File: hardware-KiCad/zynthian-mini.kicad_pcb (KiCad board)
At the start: 2 copper layers, 165 x 115 mm, 75 parts, among them SW1 SW_Push, SW10 SW_Push, SW11 SW_Push, SW12 SW_Push, SW13 SW_Push, SW14 SW_Push, SW15 SW_Push, SW16 SW_Push, SW17 SW_Push, SW18 SW_Push, SW19 SW_Push, SW2 SW_Push, SW20 SW_Push, SW3 SW_Push, SW4 SW_Push, SW5 SW_Push, SW6 SW_Push, SW7 SW_Push, SW8 SW_Push, SW9 SW_Push, U1 74HCT14, U2 H11L1M

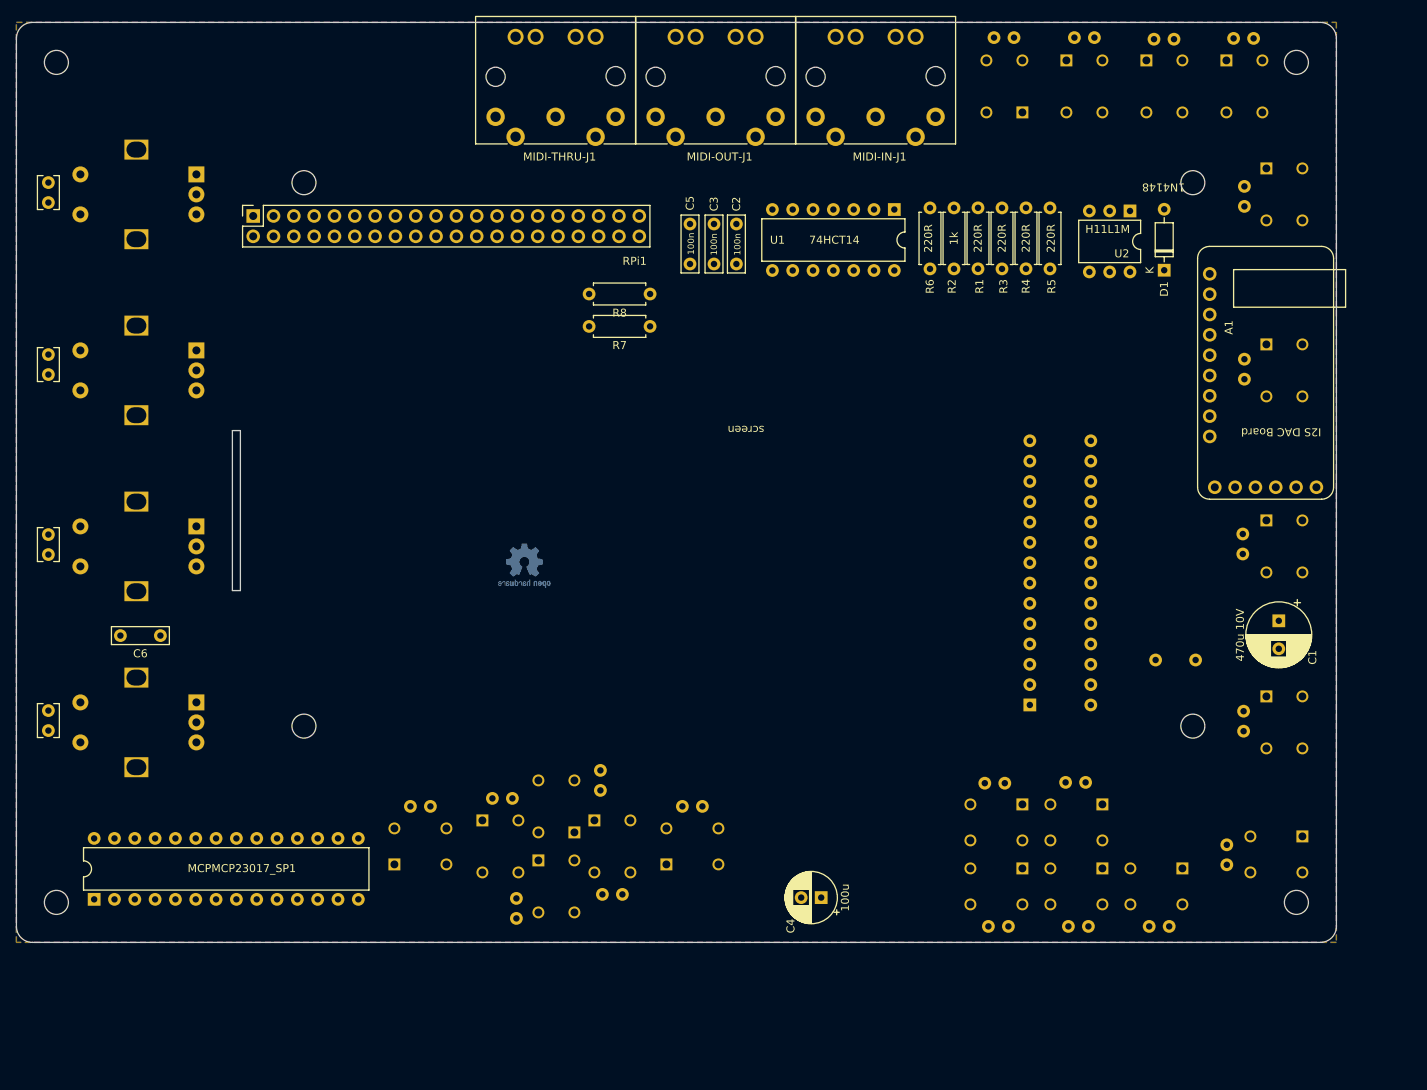
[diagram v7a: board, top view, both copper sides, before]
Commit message: first workable solution for v2 20 pins
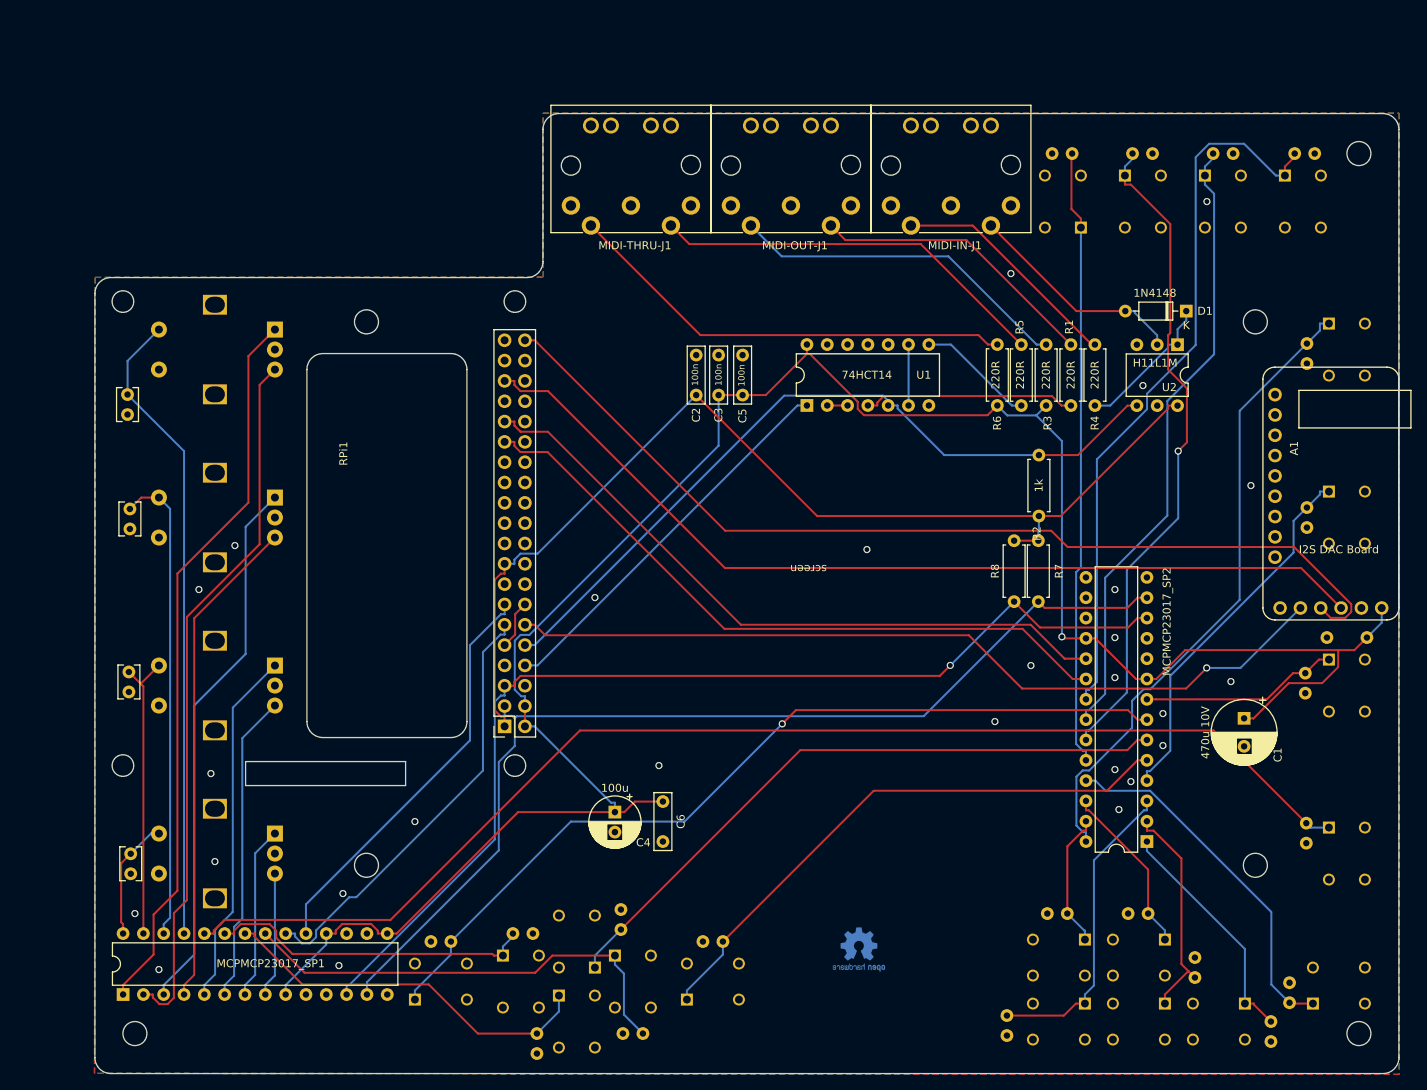
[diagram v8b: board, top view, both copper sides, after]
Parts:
- added G***: MINI v2, project-footprints:Zynthian Logo Mask, B.Cu at (131.4, 148.9)
- Enc1, Enc2, Enc3, Enc4: footprint project-footprints:RotaryEncoder_Alps_EC12E-Switch_Vertical_H20mm -> Rotary_Encoder:RotaryEncoder_Alps_EC12E-Switch_Vertical_H20mm
- MCPMCP23017_SP2: moved to F.Cu
- RPi1: footprint Connector_PinSocket_2.54mm:PinSocket_2x20_P2.54mm_Vertical -> project-footprints:raspberry pi 4 HAT
- moved C6 66.2 mm to (104.4, 121.4), turned to -90 degrees
- moved REF** 63.7 mm to (128.9, 139.9)
- moved R8 59.6 mm to (148.3, 96.4), turned to 90 degrees
- moved R7 59.5 mm to (151.3, 96.4), turned to 90 degrees
- moved R2 32.7 mm to (151.4, 85.7)
- moved RPi1 30.8 mm to (61.4, 77.9)
- moved C13 28.3 mm to (37.5, 70.5)
- moved C4 27.9 mm to (98.4, 122.7), turned to -90 degrees
- moved U1 26.8 mm to (122.4, 71.9), turned to 90 degrees
- moved C7 26.6 mm to (192.4, 100.9), turned to 180 degrees
- moved Enc1 24.2 mm to (55.9, 62.4)
- moved Enc2 23.5 mm to (55.9, 83.4)
- moved Enc3 22.8 mm to (55.9, 104.4)
- moved MCPMCP23017_SP2 22.5 mm to (164.9, 126.4), turned to 180 degrees
- moved Enc4 22.2 mm to (55.9, 125.4)
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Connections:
- D1 pad 1: (no net) -> Net-(D1-K)
- D1 pad 2: (no net) -> Net-(D1-A)
- MCPMCP23017_SP1 pad 11: (no net) -> unconnected-(MCPMCP23017_SP1-NC-Pad11)
- MCPMCP23017_SP1 pad 14: (no net) -> unconnected-(MCPMCP23017_SP1-NC-Pad14)
- MCPMCP23017_SP1 pad 19: (no net) -> INT4
- MCPMCP23017_SP1 pad 20: (no net) -> INT3
- RPi1 pad 15: (no net) -> unconnected-(RPi1-Pin_15-Pad15)
- RPi1 pad 16: (no net) -> unconnected-(RPi1-Pin_16-Pad16)
- RPi1 pad 18: (no net) -> unconnected-(RPi1-Pin_18-Pad18)
- RPi1 pad 19: (no net) -> unconnected-(RPi1-Pin_19-Pad19)
- RPi1 pad 21: (no net) -> unconnected-(RPi1-Pin_21-Pad21)
- RPi1 pad 22: (no net) -> unconnected-(RPi1-Pin_22-Pad22)
- RPi1 pad 23: (no net) -> unconnected-(RPi1-Pin_23-Pad23)
- RPi1 pad 24: (no net) -> unconnected-(RPi1-Pin_24-Pad24)
- RPi1 pad 26: (no net) -> unconnected-(RPi1-Pin_26-Pad26)
- RPi1 pad 27: (no net) -> unconnected-(RPi1-Pin_27-Pad27)
- RPi1 pad 28: (no net) -> unconnected-(RPi1-Pin_28-Pad28)
- RPi1 pad 32: (no net) -> unconnected-(RPi1-Pin_32-Pad32)
- RPi1 pad 33: (no net) -> unconnected-(RPi1-Pin_33-Pad33)
- RPi1 pad 36: (no net) -> unconnected-(RPi1-Pin_36-Pad36)
- RPi1 pad 37: (no net) -> unconnected-(RPi1-Pin_37-Pad37)
- RPi1 pad 38: (no net) -> unconnected-(RPi1-Pin_38-Pad38)
- RPi1 pad 7: (no net) -> unconnected-(RPi1-Pin_7-Pad7)
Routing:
- net +5V: track 0.00 -> 271.8 mm, vias 0 -> 1
- net SWITCH-20: track 0.00 -> 156.3 mm
- net SCK: track 0.00 -> 134.0 mm, vias 0 -> 1
- net +3.3V: track 0.00 -> 133.4 mm
- net SDA: track 0.00 -> 130.7 mm
- net I2S_AUDIO_OUT_DATA: track 0.00 -> 122.5 mm
- net I2S_LRCLK: track 0.00 -> 116.6 mm
- net SWITCH-15: track 0.00 -> 108.6 mm, vias 0 -> 1
- net I2S_BCLK: track 0.00 -> 104.4 mm, vias 0 -> 1
- net MIDI_IN: track 0.00 -> 95.9 mm
- net ENC-A-1: track 0.00 -> 91.0 mm
- net SWITCH-1: track 0.00 -> 90.4 mm
- net ENC-B-1: track 0.00 -> 88.6 mm
- net INT2: track 0.00 -> 85.2 mm
- net INT1: track 0.00 -> 85.2 mm
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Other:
- board size 165 x 115 mm -> 163 x 120 mm
